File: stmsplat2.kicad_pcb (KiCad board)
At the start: 2 copper layers, 100 x 100 mm, 103 parts, among them J1 C11_2X36, J10 Conn_01x03_Male, J11 Conn_01x02_Male, J12 Conn_01x04_Male, J13 Conn_01x04_Male, J14 Conn_01x02, J15 Conn_01x02, J16 Screw_Terminal_01x03, J17 Screw_Terminal_01x02, J2 C12_2X36, J3 Conn_01x04_Male, J4 Conn_01x04_Male, J5 Conn_Coaxial, J6 Conn_01x04_Male, J7 Conn_01x04_Male, J8 Conn_01x04_Male, J9 Conn_01x03_Male, Q1 BSS138LT1G, U1 ublox_chinese_PCB_module, U10 XCVR_E30-400M20S, U11 3115_module, U2 ESP-C3-13U, U3 SST25VF032B, U4 48L512-48LM01, U5 Opamp_Quad_MCP6024, U6 E180-ZG120A, U7 AZ1084C, U8 MCP6S93-X_UN, U9 DS2485

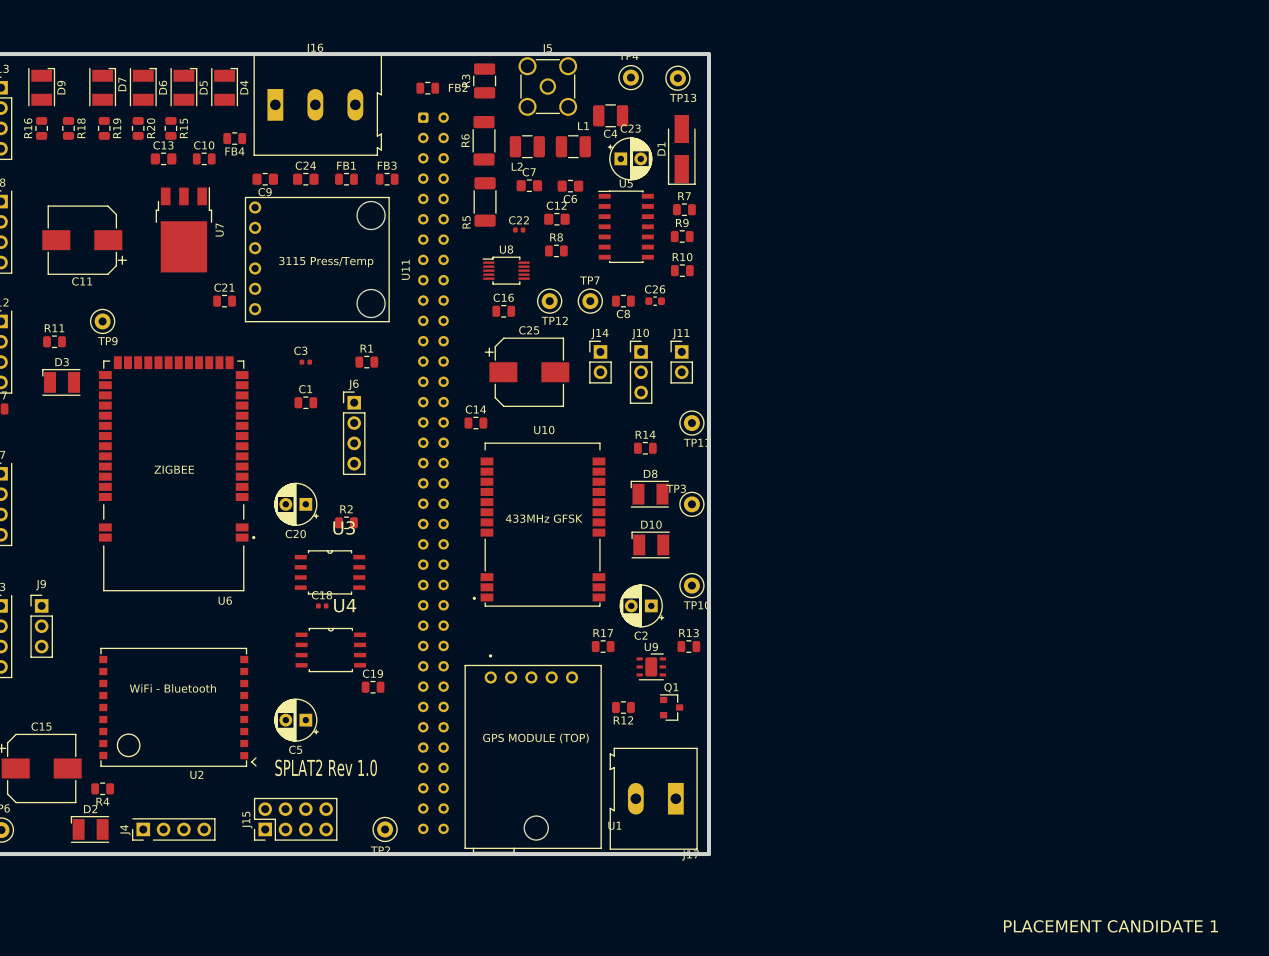
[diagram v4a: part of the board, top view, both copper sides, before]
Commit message: Added a few passives in sch. Library update may not be good? Placement tweaks.
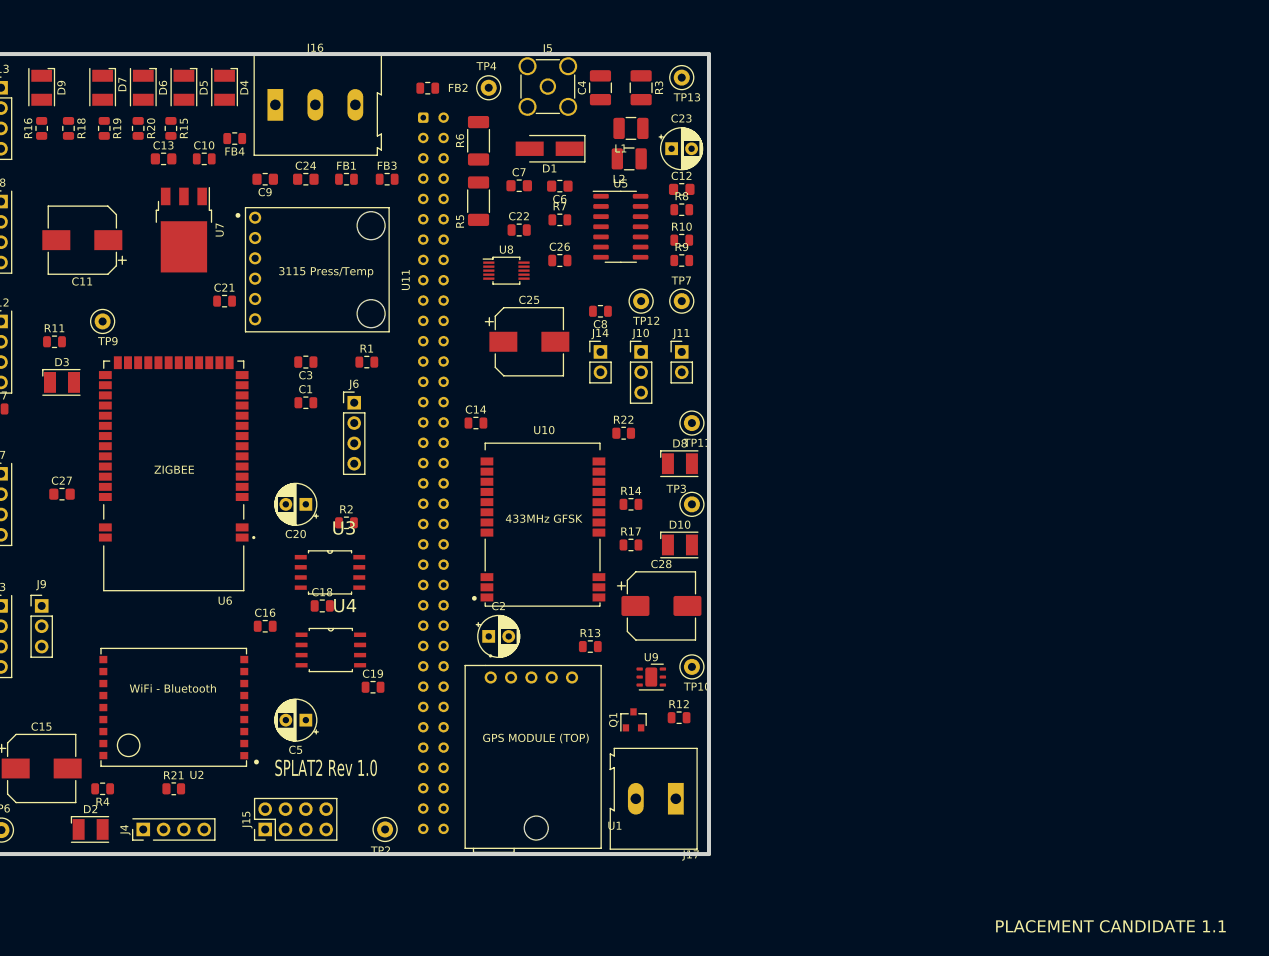
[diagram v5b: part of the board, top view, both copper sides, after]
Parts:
- added C27: 0.1uF, Capacitor_SMD:C_0805_2012Metric_Pad1.15x1.40mm_HandSolder, F.Cu at (71.1, 120.7)
- added C28: 100uF, Capacitor_SMD:CP_Elec_8x10, F.Cu at (146.1, 134.6)
- added R21: 4K7, Resistor_SMD:R_0805_2012Metric, F.Cu at (85.1, 157.5)
- added R22: 4K7, Resistor_SMD:R_0805_2012Metric, F.Cu at (141.3, 113.0)
- C18, C22, C3: footprint Capacitor_SMD:C_0402_1005Metric -> Capacitor_SMD:C_0805_2012Metric
- C26: footprint Capacitor_SMD:C_0603_1608Metric -> Capacitor_SMD:C_0805_2012Metric
- U10: value XCVR_E30-400M20S -> XCVR_E30-400M20S (Si4463)
- moved C16 49.4 mm to (96.5, 137.2)
- moved C2 20.7 mm to (124.5, 138.4), turned to 0 degrees
- moved R3 19.6 mm to (143.5, 69.8), turned to 270 degrees
- moved TP4 17.8 mm to (124.5, 69.8)
- moved D1 16.5 mm to (132.1, 77.5), turned to 180 degrees
- moved R8 16.5 mm to (148.6, 85.1)
- moved C12 16.0 mm to (148.6, 82.5)
- moved R7 15.6 mm to (133.3, 86.4)
- moved R17 13.2 mm to (142.2, 127.0)
- moved C26 13.0 mm to (133.3, 91.4)
- moved L2 12.8 mm to (142.0, 78.7)
- moved R13 12.3 mm to (137.2, 139.7)
- moved TP7 11.4 mm to (148.6, 96.5)
- moved TP12 11.4 mm to (143.5, 96.5)
- moved TP10 10.2 mm to (149.9, 142.2)
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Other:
- net class 40thou added: clearance 0.2, trace_width 1.016, via_dia 0.8, via_drill 0.762
- net class 80thou added: clearance 0.2, trace_width 2.032, via_dia 0.8, via_drill 0.4
- board text added: "PLACEMENT CANDIDATE 1.1"
- board text removed: "PLACEMENT CANDIDATE 1"
